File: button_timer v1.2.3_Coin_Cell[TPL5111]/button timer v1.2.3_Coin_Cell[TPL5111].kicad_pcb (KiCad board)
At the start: 2 copper layers, 21 x 47.8 mm, 25 parts, among them J1 Conn_01x05_Female, Q1 IRF540N, SW1 SW_Push, SW2 SW_Push, U1 TPS61097A, U3 TPL5111, X1 ESP-12E

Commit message: Silkscreen Update
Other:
- board text added: "Button - Coin Cell v.1.2.3 TPL5111"
- board text removed: "Button - Coin Cell v.1.2.1"

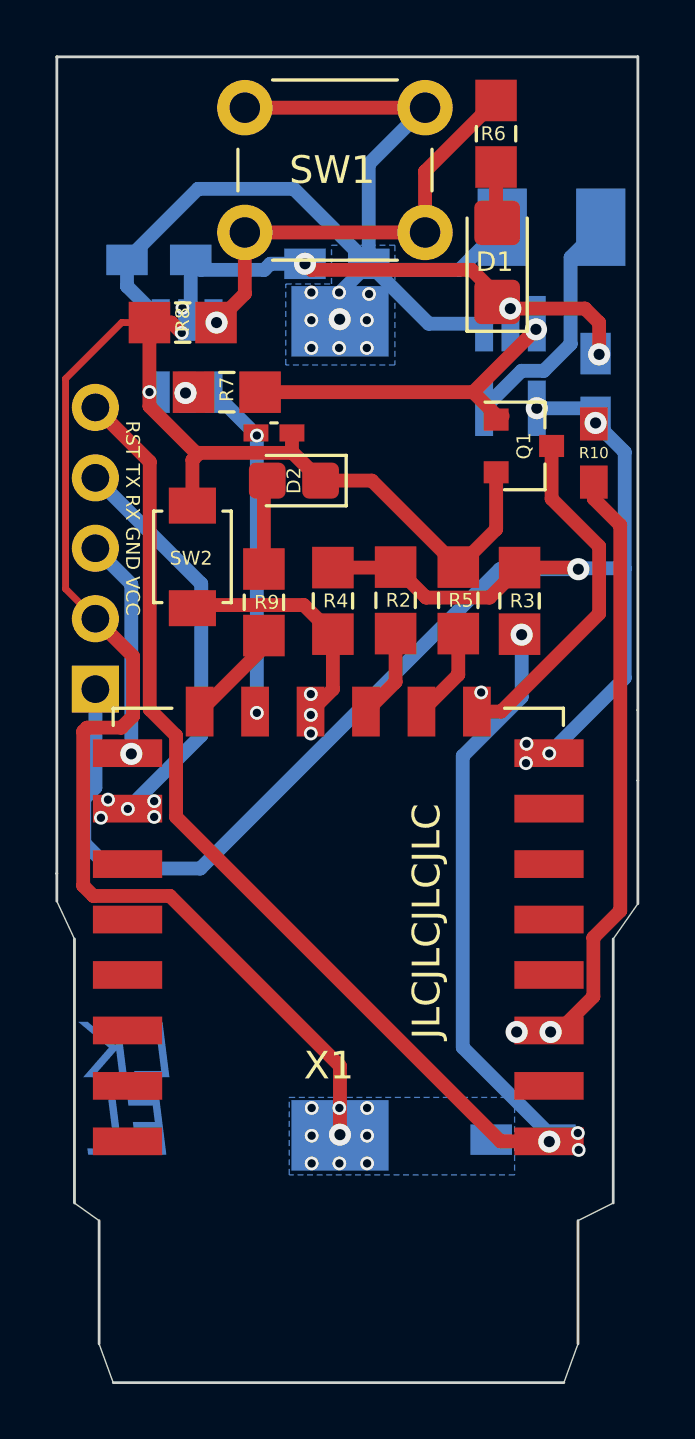
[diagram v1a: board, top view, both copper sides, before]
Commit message: cap between esp vcc and ground added
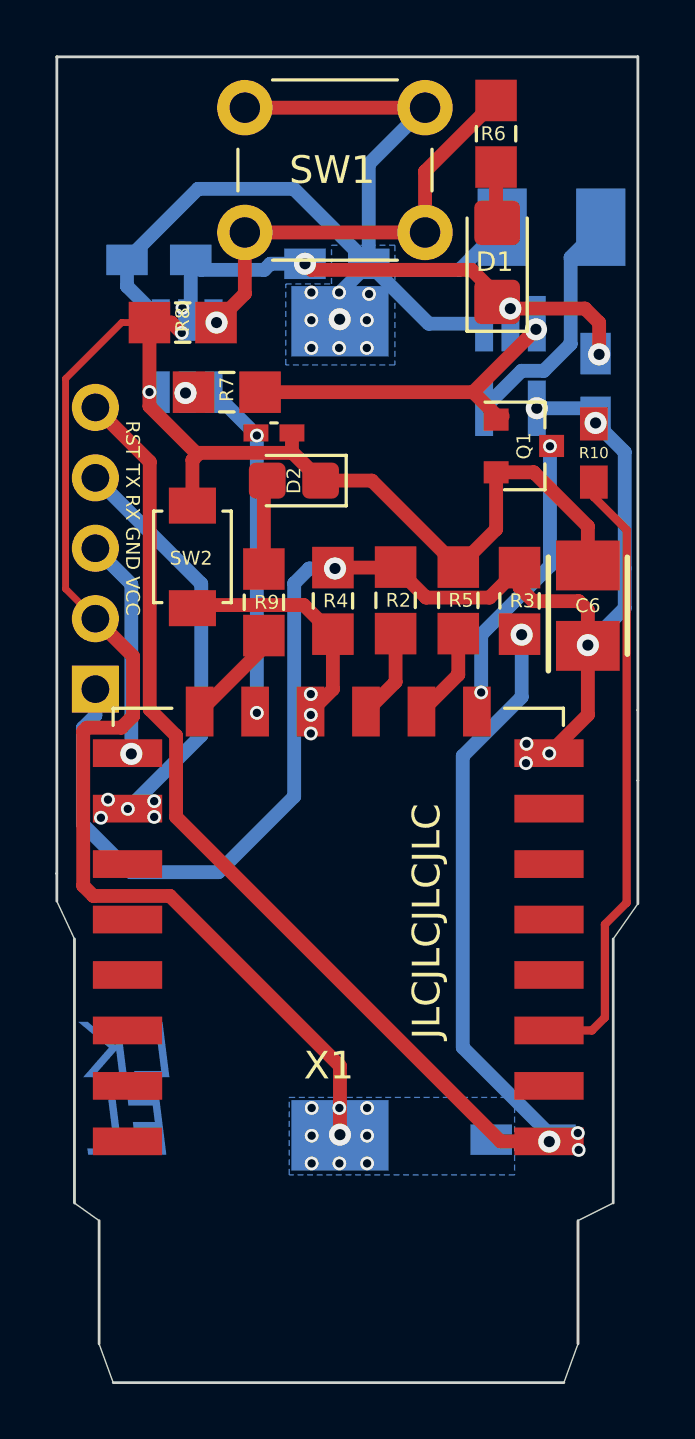
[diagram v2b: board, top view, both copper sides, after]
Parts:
- added C6: TAJB476M010TNJ, SamacSys_Parts:CAPPM3528X210N, F.Cu at (134.7, 74.3)
- Q1: value IRF540N -> mmbt2222
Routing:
- net /GND: track 84.7 -> 90.2 mm
- net /VCC: track 55.8 -> 52.3 mm, vias 6 -> 7
- net /GND_ESP: track 12.6 -> 9.91 mm, vias 1 -> 2
- net /EN: track 22.7 -> 22.3 mm, vias 2 -> 0

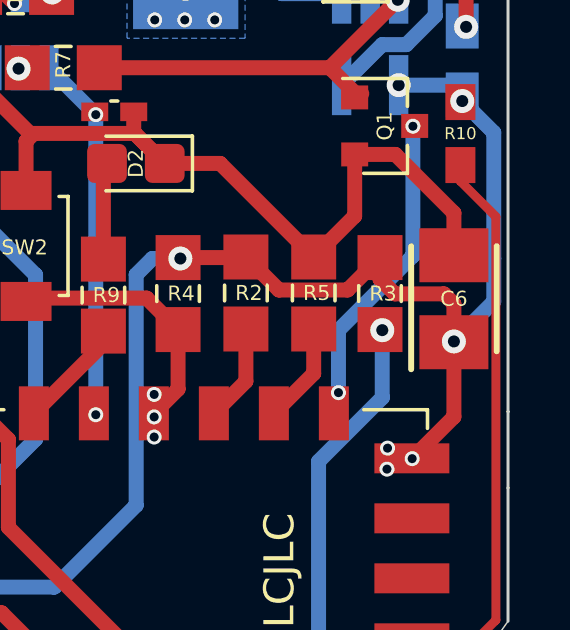
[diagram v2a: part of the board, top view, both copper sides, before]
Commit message: Added 100nF decoupling capacitors between VCC and Ground of the ESP
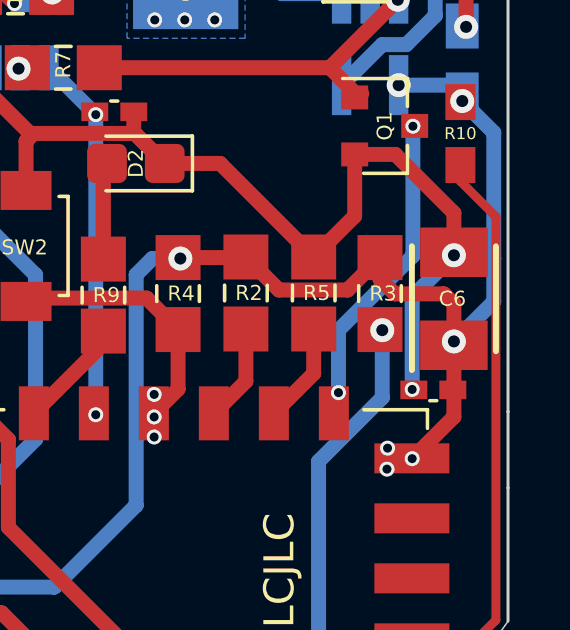
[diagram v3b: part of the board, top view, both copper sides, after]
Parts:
- added C7: 100nF, handsolder:C_0402_1005Metric_Pad0.74x0.62mm_HandSoldermod, F.Cu at (134.0, 77.4)
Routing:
- net /GND: track 90.2 -> 95.3 mm, vias 15 -> 17
